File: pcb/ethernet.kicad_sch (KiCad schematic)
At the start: 39 parts, among them J4 RJ45_Hanrun_HR911105A_Horizon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, U9 W5500, Y1 25MHz

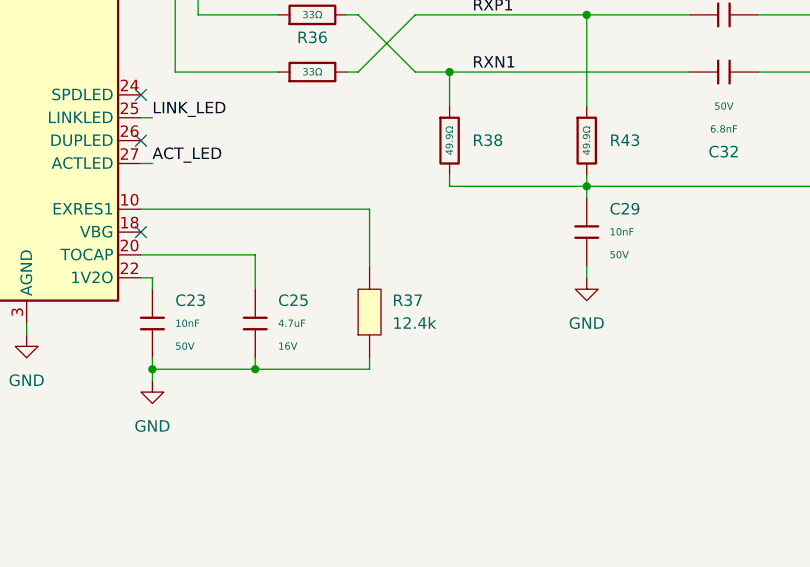
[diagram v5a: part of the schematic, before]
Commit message: feat: replace many parts for basic parts
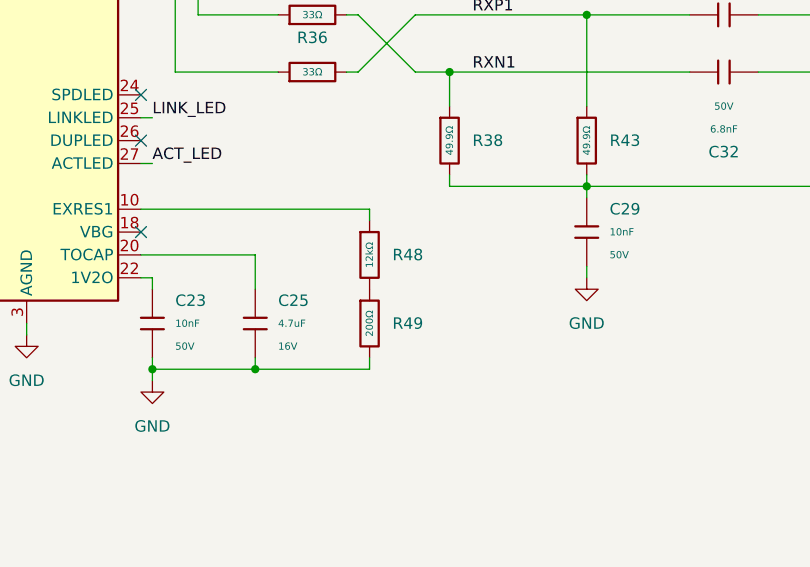
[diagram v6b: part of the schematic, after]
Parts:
- removed R37: 12.4k, EasyEDA:R0603, symbol EasyEDA:FRC0603F1242TS
- added R48: 12kΩ, PCM_JLCPCB:R_0603, symbol PCM_JLCPCB-Resistors:0603,12kΩ
- added R49: 200Ω, PCM_JLCPCB:R_0603, symbol PCM_JLCPCB-Resistors:0603,200Ω
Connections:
- net GND: now also R49.2
- net at U9.10 (EXRES1): now also R48.1
- new net: R48.2, R49.1

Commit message: pcb: update symbols and footprints to fix drc
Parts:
- C17, C18: Stock 253196 -> 651661
- C19, C33: Price 0.021USD -> 0.020USD; Stock 3388297 -> 3475471
- C20, C22, C24, C26, C27, C28, C30: Stock 70324515 -> 37493696
- C21: Price 0.011USD -> 0.012USD; Stock 2094039 -> 3193587
- C23, C29: Price 0.005USD -> 0.006USD; Stock 5921160 -> 2223405
- C25: Stock 4246728 -> 5643370
- C31, C32: Price 0.006USD -> 0.007USD; Stock 135842 -> 491854
- C34: Stock 746157 -> 1647364
- R31: Price 0.004USD -> 0.005USD; Stock 3961571 -> 4092207
- R32: Price 0.004USD -> 0.005USD; Stock 7706573 -> 13902554
- R33, R34, R35, R36: Price 0.004USD -> 0.005USD; Stock 2319032 -> 2873644
- R38, R42, R43, R44: Price 0.004USD -> 0.005USD; Stock 983409 -> 1586884
- R39, R40, R41: Price 0.004USD -> 0.005USD; Stock 51181774 -> 22319909
- R45: Price 0.004USD -> 0.005USD; Stock 5764851 -> 2613887
- R46, R47: Price 0.004USD -> 0.005USD; Stock 2977706 -> 3511720
- R48: Price 0.004USD -> 0.005USD; Stock 998337 -> 1125311
- R49: Price 0.004USD -> 0.005USD; Stock 2444311 -> 1041103
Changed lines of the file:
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@@
 			)
 		)
-		(property "Stock" "51181774"
+		(property "Stock" "22319909"
 			(at 137.16 189.23 0)
 			(hide yes)
@@
 			)
 		)
-		(property "Price" "0.004USD"
+		(property "Price" "0.005USD"
 			(at 137.16 189.23 0)
 			(hide yes)
@@
 			)
 		)
-		(property "Stock" "2094039"
+		(property "Stock" "3193587"
 			(at 88.9 181.61 0)
 			(hide yes)
@@
 			)
 		)
-		(property "Price" "0.011USD"
+		(property "Price" "0.012USD"
 			(at 88.9 181.61 0)
 			(hide yes)
@@
 			)
 		)
-		(property "Stock" "746157"
+		(property "Stock" "1647364"
 			(at 175.26 78.74 0)
 			(hide yes)
@@
 			)
 		)
-		(property "Stock" "2319032"
+		(property "Stock" "2873644"
 			(at 118.11 90.17 0)
 			(hide yes)
@@
 			)
 		)
-		(property "Price" "0.004USD"
+		(property "Price" "0.005USD"
 			(at 118.11 90.17 0)
 			(hide yes)
@@
 			)
 		)
-		(property "Stock" "70324515"
+		(property "Stock" "37493696"
 			(at 129.54 34.29 0)
 			(hide yes)
@@
 			)
 		)
-		(property "Stock" "135842"
+		(property "Stock" "491854"
 			(at 163.83 96.52 0)
 			(hide yes)
@@
 			)
 		)
-		(property "Price" "0.006USD"
+		(property "Price" "0.007USD"
 			(at 163.83 96.52 0)
 			(hide yes)
@@
 			)
 		)
-		(property "Stock" "2319032"
+		(property "Stock" "2873644"
 			(at 118.11 68.58 0)
 			(hide yes)
@@
 			)
 		)
-		(property "Price" "0.004USD"
+		(property "Price" "0.005USD"
 			(at 118.11 68.58 0)
 			(hide yes)
@@
 			)
 		)
-		(property "Stock" "5921160"
+		(property "Stock" "2223405"
 			(at 148.59 114.3 0)
 			(hide yes)
@@
 			)
 		)
-		(property "Price" "0.005USD"
+		(property "Price" "0.006USD"
 			(at 148.59 114.3 0)
 			(hide yes)
@@
 			)
 		)
-		(property "Stock" "983409"
+		(property "Stock" "1586884"
 			(at 160.02 62.23 0)
 			(hide yes)
@@
 			)
 		)
-		(property "Price" "0.004USD"
+		(property "Price" "0.005USD"
 			(at 160.02 62.23 0)
 			(hide yes)
@@
 			)
 		)
-		(property "Stock" "253196"
+		(property "Stock" "651661"
 			(at 48.26 121.92 0)
 			(hide yes)
@@
 			)
 		)
-		(property "Stock" "2319032"
+		(property "Stock" "2873644"
 			(at 118.11 96.52 0)
 			(hide yes)
@@
 			)
 		)
-		(property "Price" "0.004USD"
+		(property "Price" "0.005USD"
 			(at 118.11 96.52 0)
 			(hide yes)
@@
 			)
 		)
-		(property "Stock" "2977706"
+		(property "Stock" "3511720"
 			(at 250.19 71.12 0)
 			(hide yes)
@@
 			)
 		)
-		(property "Price" "0.004USD"
+		(property "Price" "0.005USD"
 			(at 250.19 71.12 0)
 			(hide yes)
@@
 			)
 		)
-		(property "Stock" "998337"
+		(property "Stock" "1125311"
 			(at 124.46 116.84 0)
 			(hide yes)
@@
 			)
 		)
-		(property "Price" "0.004USD"
+		(property "Price" "0.005USD"
 			(at 124.46 116.84 0)
 			(hide yes)
@@
 			)
 		)
-		(property "Stock" "70324515"
+		(property "Stock" "37493696"
 			(at 154.94 34.29 0)
 			(hide yes)
@@
 			)
 		)
-		(property "Stock" "51181774"
+		(property "Stock" "22319909"
 			(at 137.16 181.61 0)
 			(hide yes)
@@
 			)
 		)
-		(property "Price" "0.004USD"
+		(property "Price" "0.005USD"
 			(at 137.16 181.61 0)
 			(hide yes)
@@
 			)
 		)
-		(property "Stock" "2977706"
+		(property "Stock" "3511720"
 			(at 250.19 81.28 0)
 			(hide yes)
@@
 			)
 		)
-		(property "Price" "0.004USD"
+		(property "Price" "0.005USD"
 			(at 250.19 81.28 0)
 			(hide yes)
@@
 			)
 		)
-		(property "Stock" "3388297"
+		(property "Stock" "3475471"
 			(at 166.37 34.29 0)
 			(hide yes)
@@
 			)
 		)
-		(property "Price" "0.021USD"
+		(property "Price" "0.020USD"
 			(at 166.37 34.29 0)
 			(hide yes)
@@
 			)
 		)
-		(property "Stock" "70324515"
+		(property "Stock" "37493696"
 			(at 104.14 34.29 0)
 			(hide yes)
@@
 			)
 		)
-		(property "Stock" "983409"
+		(property "Stock" "1586884"
 			(at 148.59 104.14 0)
 			(hide yes)
@@
 			)
 		)
-		(property "Price" "0.004USD"
+		(property "Price" "0.005USD"
 			(at 148.59 104.14 0)
 			(hide yes)
@@
 			)
 		)
-		(property "Stock" "70324515"
+		(property "Stock" "37493696"
 			(at 91.44 34.29 0)
 			(hide yes)
@@
 			)
 		)
-		(property "Stock" "5764851"
+		(property "Stock" "2613887"
 			(at 175.26 62.23 0)
 			(hide yes)
@@
 			)
 		)
-		(property "Price" "0.004USD"
+		(property "Price" "0.005USD"
 			(at 175.26 62.23 0)
 			(hide yes)
@@
 			)
 		)
-		(property "Stock" "70324515"
+		(property "Stock" "37493696"
 			(at 142.24 34.29 0)
 			(hide yes)
@@
 			)
 		)
-		(property "Stock" "51181774"
+		(property "Stock" "22319909"
 			(at 137.16 173.99 0)
 			(hide yes)
@@
 			)
 		)
-		(property "Price" "0.004USD"
+		(property "Price" "0.005USD"
 			(at 137.16 173.99 0)
 			(hide yes)
@@
 			)
 		)
-		(property "Stock" "70324515"
+		(property "Stock" "37493696"
 			(at 116.84 34.29 0)
 			(hide yes)
@@
 			)
 		)
-		(property "Stock" "3388297"
+		(property "Stock" "3475471"
 			(at 59.69 34.29 0)
 			(hide yes)
@@
 			)
 		)
-		(property "Price" "0.021USD"
+		(property "Price" "0.020USD"
 			(at 59.69 34.29 0)
 			(hide yes)
@@
 			)
 		)
-		(property "Stock" "3961571"
+		(property "Stock" "4092207"
 			(at 38.1 104.14 0)
 			(hide yes)
@@
 			)
 		)
-		(property "Price" "0.004USD"
+		(property "Price" "0.005USD"
 			(at 38.1 104.14 0)
 			(hide yes)
@@
 			)
 		)
-		(property "Stock" "135842"
+		(property "Stock" "491854"
 			(at 163.83 90.17 0)
 			(hide yes)
@@
 			)
 		)
-		(property "Price" "0.006USD"
+		(property "Price" "0.007USD"
 			(at 163.83 90.17 0)
 			(hide yes)
@@
 			)
 		)
-		(property "Stock" "2319032"
+		(property "Stock" "2873644"
 			(at 118.11 74.93 0)
 			(hide yes)
@@
 			)
 		)
-		(property "Price" "0.004USD"
+		(property "Price" "0.005USD"
 			(at 118.11 74.93 0)
 			(hide yes)
@@
 			)
 		)
-		(property "Stock" "5921160"
+		(property "Stock" "2223405"
 			(at 100.33 124.46 0)
 			(hide yes)
@@
 			)
 		)
-		(property "Price" "0.005USD"
+		(property "Price" "0.006USD"
 			(at 100.33 124.46 0)
 			(hide yes)
@@
 			)
 		)
-		(property "Stock" "983409"
+		(property "Stock" "1586884"
 			(at 144.78 62.23 0)
 			(hide yes)
@@
 			)
 		)
-		(property "Price" "0.004USD"
+		(property "Price" "0.005USD"
 			(at 144.78 62.23 0)
 			(hide yes)
@@
 			)
 		)
-		(property "Stock" "70324515"
+		(property "Stock" "37493696"
 			(at 71.12 34.29 0)
 			(hide yes)
@@
 			)
 		)
-		(property "Stock" "2444311"
+		(property "Stock" "1041103"
 			(at 124.46 124.46 0)
 			(hide yes)
@@
 			)
 		)
-		(property "Price" "0.004USD"
+		(property "Price" "0.005USD"
 			(at 124.46 124.46 0)
 			(hide yes)
@@
 			)
 		)
-		(property "Stock" "983409"
+		(property "Stock" "1586884"
 			(at 133.35 104.14 0)
 			(hide yes)
@@
 			)
 		)
-		(property "Price" "0.004USD"
+		(property "Price" "0.005USD"
 			(at 133.35 104.14 0)
 			(hide yes)
@@
 			)
 		)
-		(property "Stock" "4246728"
+		(property "Stock" "5643370"
 			(at 111.76 124.46 0)
 			(hide yes)
@@
 			)
 		)
-		(property "Stock" "7706573"
+		(property "Stock" "13902554"
 			(at 48.26 111.76 0)
 			(hide yes)
@@
 			)
 		)
-		(property "Price" "0.004USD"
+		(property "Price" "0.005USD"
 			(at 48.26 111.76 0)
 			(hide yes)
@@
 			)
 		)
-		(property "Stock" "253196"
+		(property "Stock" "651661"
 			(at 27.94 121.92 0)
 			(hide yes)

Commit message: pcb: update drifted oscillator footprint
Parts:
- Y1: footprint PCM_JLCPCB:OSC-SMD_4P-L3.2-W2.5-BL -> EasyEDA:OSC-SMD_4P-L3.2-W2.5-BL; symbol Device:Crystal_GND24 -> EasyEDA:Crystal_GND24
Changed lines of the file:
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@@
 	)
 	(symbol
-		(lib_id "Device:Crystal_GND24")
+		(lib_id "EasyEDA:Crystal_GND24")
 		(at 38.1 116.84 0)
 		(unit 1)
@@
 			)
 		)
-		(property "Footprint" "PCM_JLCPCB:OSC-SMD_4P-L3.2-W2.5-BL"
+		(property "Footprint" "EasyEDA:OSC-SMD_4P-L3.2-W2.5-BL"
 			(at 38.1 116.84 0)
 			(hide yes)
